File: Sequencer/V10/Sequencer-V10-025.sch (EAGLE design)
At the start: 42 parts, among them IC2 LD117ADT50TR, IC6 LM1117MPX-ADJ, Q1 IRF530, X1 MARTIN8X2-1751303, X2 MARTIN3X2-1751303175L303-3, X3 MARTIN8X2-1751303, X4 1751264, X5 MARTIN3X2-1751303175L303-3

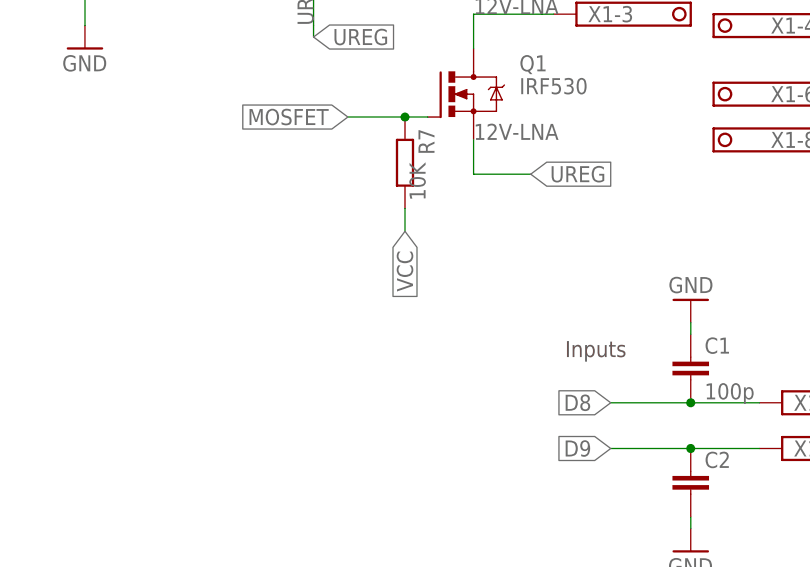
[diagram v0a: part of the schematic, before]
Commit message: Fix MOSFET to UREG
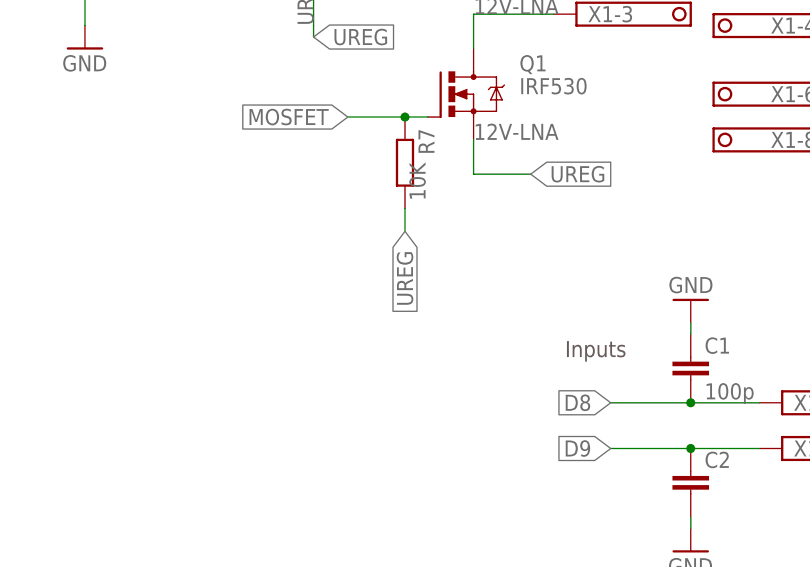
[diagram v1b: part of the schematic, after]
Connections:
- net UREG: now also R7.2
- net VCC: no longer R7.2
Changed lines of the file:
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@@
 <label x="92.71" y="175.26" size="1.778" layer="95" xref="yes"/>
+</segment>
+<segment>
+<pinref part="R7" gate="G$1" pin="2"/>
+<wire x1="102.87" y1="153.67" x2="102.87" y2="156.21" width="0.1524" layer="91"/>
+<label x="102.87" y="153.67" size="1.778" layer="95" rot="R270" xref="yes"/>
 </segment>
 </net>
@@
 <junction x="50.8" y="101.6"/>
 </segment>
-<segment>
-<pinref part="R7" gate="G$1" pin="2"/>
-<wire x1="102.87" y1="153.67" x2="102.87" y2="156.21" width="0.1524" layer="91"/>
-<label x="102.87" y="153.67" size="1.778" layer="95" rot="R270" xref="yes"/>
-</segment>
 </net>
